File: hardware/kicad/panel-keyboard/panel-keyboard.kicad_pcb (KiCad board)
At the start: 2 copper layers, 120 x 120 mm, 79 parts, among them J2 SWD (DNP), J485 KF2EDGV-5.08-3P, SW1 Tact_12mm, SW10 Tact_12mm, SW11 Tact_12mm, SW12 Tact_12mm, SW13 Tact_12mm, SW14 Tact_12mm, SW15 Tact_12mm, SW16 Tact_12mm, SW2 Tact_12mm, SW3 Tact_12mm, SW4 Tact_12mm, SW5 Tact_12mm, SW6 Tact_12mm, SW7 Tact_12mm, SW8 Tact_12mm, SW9 Tact_12mm, U1 STM32G030F6P6, U3 SIT3485 / MAX3485, U4 XL1509-5.0E1, U5 AMS1117-3.3, U6 TM1638

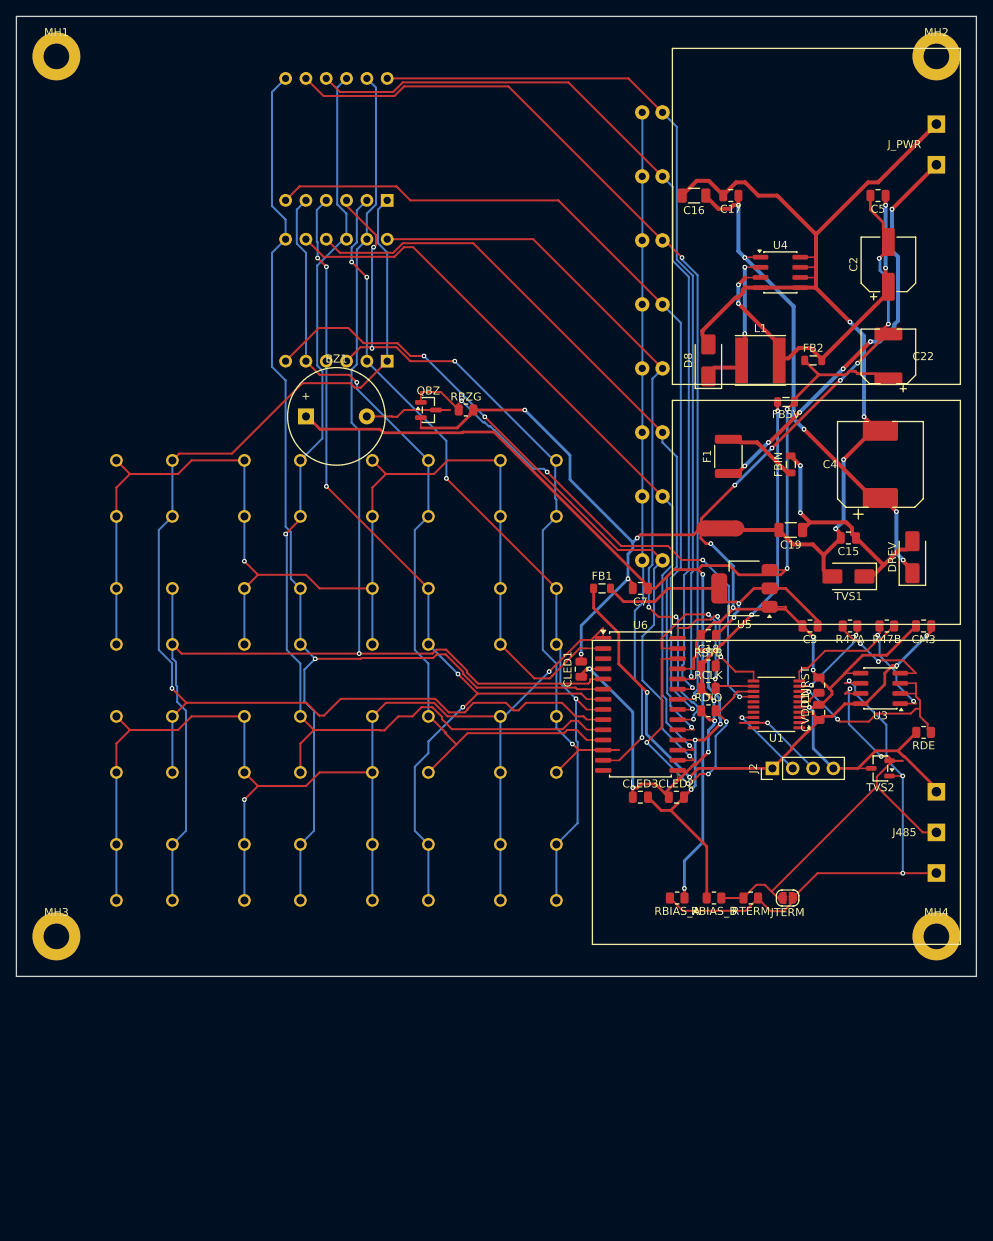
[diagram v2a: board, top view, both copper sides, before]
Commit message: tạo c# app, update firmware để bàn phím hỗ trợ cả 2 mode slave/master. hỗ trợ giắc nạp và debug trên board phù hợp với mạch nạp DAPLINK STM32 cổng Type-C
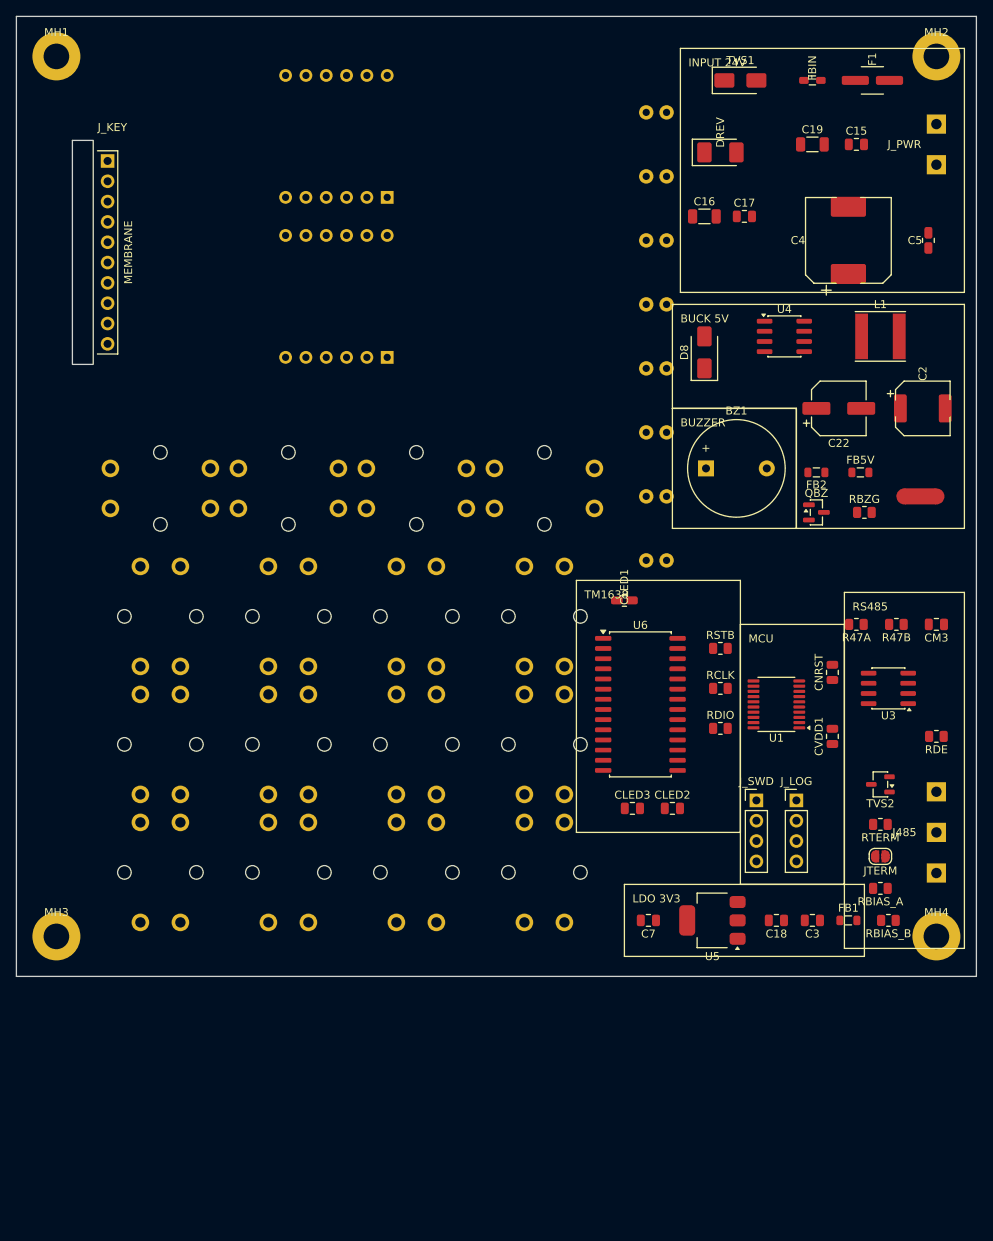
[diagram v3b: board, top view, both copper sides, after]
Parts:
- removed J2: SWD (DNP), PinHeader_1x04_P2.54mm_Vertical
- added J_KEY: Membrane 1x10 2.54, Membrane_1x10_P2.54_Vertical_Slot, F.Cu at (11.4, 18.1)
- added J_LOG: PinHeader_1x04_P2.54mm_Vertical, PinHeader_1x04_P2.54mm_Vertical, F.Cu at (97.5, 98.0)
- added J_SWD: PinHeader_1x04_P2.54mm_Vertical, PinHeader_1x04_P2.54mm_Vertical, F.Cu at (92.5, 98.0)
- C16, C19: value 10uF 50V -> 2.2uF 50V X7R
- C2, C22: value 220uF 10V -> 220uF 10V RVT1A221M0605
- C4: value 470uF 35V -> 470uF 35V RVT1V471M1010
- F1: value PPTC 1812 0.5A 33V -> mSMD050-33V (PPTC 0.5A 33V)
- FB1, FB2, FB5V: value 120R@100MHz 2A -> GZ2012D101TF 100R
- FBIN: value 600R@100MHz 2A -> GZ2012D601TF 600R
- J485: value KF2EDGV-5.08-3P -> KF301-5.08-3P
- J_PWR: value KF2EDGV-5.08-2P -> KF301-5.08-2P
- L1: value 47uH 6045 -> SWPA6045S470MT 47uH
- SW1, SW10, SW11, SW12, SW13, SW14, SW15, SW16, SW2, SW3, SW4, SW5, SW6, SW7, SW8, SW9: value Tact_12mm -> B3F-4055
- TVS1: value SMAJ28A -> SMAJ28CA
- TVS2: value SM712 -> PSM712-LF-T7
- U3: value SIT3485 / MAX3485 -> SP3485EN
- moved TVS1 63.5 mm to (90.5, 8.00), turned to 0 degrees
- moved DREV 56.0 mm to (88.0, 17.0), turned to 0 degrees
- moved FB1 51.7 mm to (104.0, 113.0)
- moved RBZG 51.4 mm to (106.0, 62.0)
- moved BZ1 50.4 mm to (86.2, 56.5)
- moved F1 50.3 mm to (107.0, 8.00), turned to 0 degrees
- moved QBZ 50.2 mm to (100.0, 62.0)
- moved C15 49.2 mm to (105.0, 16.0), turned to 0 degrees
- moved C19 48.3 mm to (99.5, 16.0), turned to 0 degrees
- moved FBIN 48.1 mm to (99.5, 8.00), turned to 0 degrees
- moved U5 41.7 mm to (87.0, 113.0)
- moved C7 41.5 mm to (79.0, 113.0)
- moved C3 36.8 mm to (99.5, 113.0)
- moved C18 36.6 mm to (95.0, 113.0)
- moved C4 28.3 mm to (104.0, 28.0)
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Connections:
- JTERM pad 2: RS485_B_BUS -> RS485_TERM
- RTERM pad 1: RS485_A_BUS -> RS485_TERM
- U1 pad 1: (no net) -> LOG_RX
- U1 pad 20: (no net) -> LOG_TX
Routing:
- net GND: track 253.5 -> 0.00 mm, vias 19 -> 0
- net SEG1: track 171.3 -> 0.00 mm, vias 1 -> 0
- net KEY_K1: track 161.0 -> 0.00 mm, vias 2 -> 0
- net KEY_K2: track 157.4 -> 0.00 mm, vias 1 -> 0
- net SEG5: track 151.9 -> 0.00 mm, vias 1 -> 0
- net +5V: track 151.4 -> 0.00 mm, vias 4 -> 0
- net SEG2: track 147.1 -> 0.00 mm, vias 1 -> 0
- net SEG6: track 133.4 -> 0.00 mm, vias 1 -> 0
- net GND_PWR: track 126.3 -> 0.00 mm, vias 4 -> 0
- net GRID_2: track 116.6 -> 0.00 mm, vias 1 -> 0
- net SEG3: track 116.4 -> 0.00 mm, vias 5 -> 0
- net GRID_3: track 115.5 -> 0.00 mm, vias 2 -> 0
- net GRID_1: track 110.9 -> 0.00 mm, vias 1 -> 0
- net GRID_4: track 109.4 -> 0.00 mm, vias 1 -> 0
- net SEG4: track 105.1 -> 0.00 mm, vias 4 -> 0
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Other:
- board text added: "BUCK 5V"
- board text added: "BUZZER"
- board text added: "INPUT 24V"
- board text added: "LDO 3V3"
- board text added: "MCU"
- board text added: "RS485"
- board text added: "TM1638"
